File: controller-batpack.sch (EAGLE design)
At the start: 7 parts

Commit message: updated board with display and battery
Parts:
- removed 4D_LLC, RF_LLC: (no value), con-lstb:MA06-2
- removed BAT: SL-160AA/PR, battery:SL-160AA/PR
- removed RF_IC: MRF24J40, microchip:MRF24J40
- removed VD_R1: 1k, resistor:R-EU_0204/5
- removed VD_R2: 2k, resistor:R-EU_0204/5
- added G1: 5V, battery:SL-160AA/PR
- added JP1: (no value), pinhead:PINHD-1X8
- added R1: 2k, rcl:R-EU_0204/5
- added R2: 1k, rcl:R-EU_0204/5
- added U$1: LEVEL-SHIFTER-4CH, diy-modules:LEVEL-SHIFTER-4CH
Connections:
- removed net N$1: BAT.-, VD_R2.1
- removed net N$2: BAT.+, VD_R1.1
- removed net N$3: 4D_IC.1, RF_IC.VDD, VD_R1.2, VD_R2.2
- new net 3.3V: 4D_IC.1, R1.1, R2.2
- new net 4D_CS: JP1.4, U$1.HV2
- new net 4D_CS_L: 4D_IC.5, U$1.LV2
- new net 4D_INT: 4D_IC.6, JP1.5
- new net 4D_PD: JP1.3, U$1.HV1
- new net 4D_PD_L: 4D_IC.7, U$1.LV1
- new net 5V: G1.+, JP1.1, R2.1, U$1.HV
- new net GND: 4D_IC.10, G1.-, JP1.2, R1.2
- new net MISO: 4D_IC.3, JP1.6
- new net MOSI: JP1.7, U$1.HV3
- new net MOSI_L: 4D_IC.4, U$1.LV3
- new net N$10: U$1.LV
- new net SCK: JP1.8, U$1.HV4
- new net SCK_L: 4D_IC.2, U$1.LV4
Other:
- moved on the sheet: 4D_IC

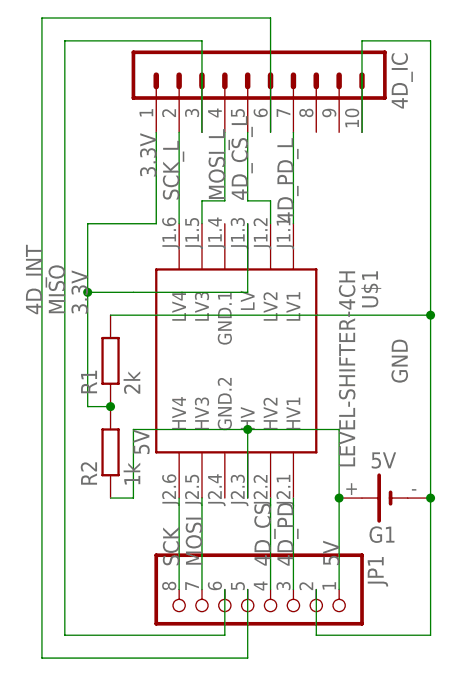
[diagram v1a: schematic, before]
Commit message: added pcb design and got rid of llc in battery pack
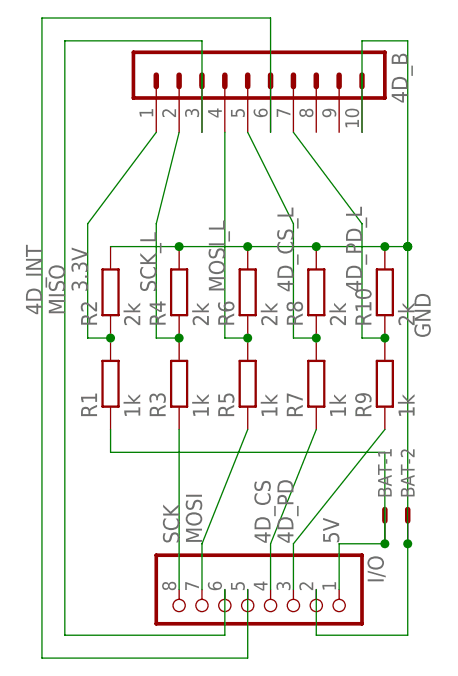
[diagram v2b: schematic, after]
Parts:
- removed G1: 5V, battery:SL-160AA/PR
- removed U$1: LEVEL-SHIFTER-4CH, diy-modules:LEVEL-SHIFTER-4CH
- added BAT: 22-23-2021, con-molex:22-23-2021
- added R10, R4, R6, R8: 2k, rcl:R-EU_M1206
- added R3, R5, R7, R9: 1k, rcl:R-EU_M1206
- R1: value 2k -> 1k; device rcl:R-EU_0204/5 -> rcl:R-EU_M1206
- R2: value 1k -> 2k; device rcl:R-EU_0204/5 -> rcl:R-EU_M1206
- renumbered 4D_IC to 4D_B, JP1 to I/O
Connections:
- removed net N$10: U$1.LV
- net 3.3V: now also R1.2, R2.1; no longer R1.1, R2.2
- net 4D_CS: now also R7.1; no longer U$1.HV2
- net 4D_CS_L: now also R7.2, R8.1; no longer U$1.LV2
- net 4D_PD: now also R9.1; no longer U$1.HV1
- net 4D_PD_L: now also R10.1, R9.2; no longer U$1.LV1
- net 5V: now also BAT-1.S, R1.1; no longer G1.+, R2.1, U$1.HV
- net GND: now also BAT-2.S, R10.2, R2.2, R4.2, R6.2, R8.2; no longer G1.-, R1.2
- net MOSI: now also R5.1; no longer U$1.HV3
- net MOSI_L: now also R5.2, R6.1; no longer U$1.LV3
- net SCK: now also R3.1; no longer U$1.HV4
- net SCK_L: now also R3.2, R4.1; no longer U$1.LV4
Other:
- moved on the sheet: R1, R2

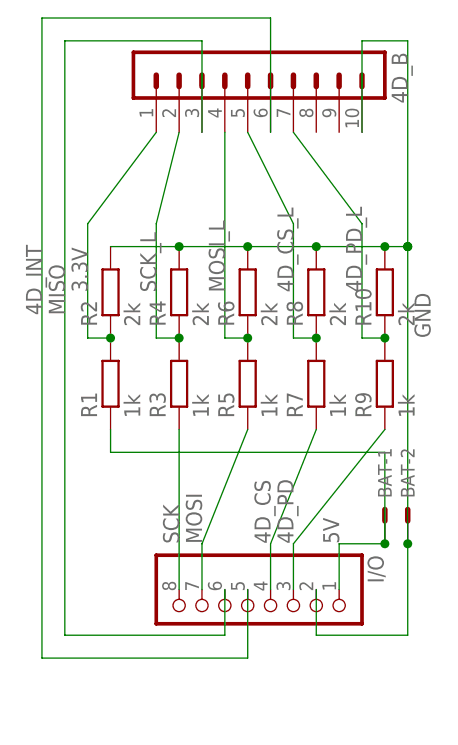
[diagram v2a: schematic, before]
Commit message: updated battery pack board
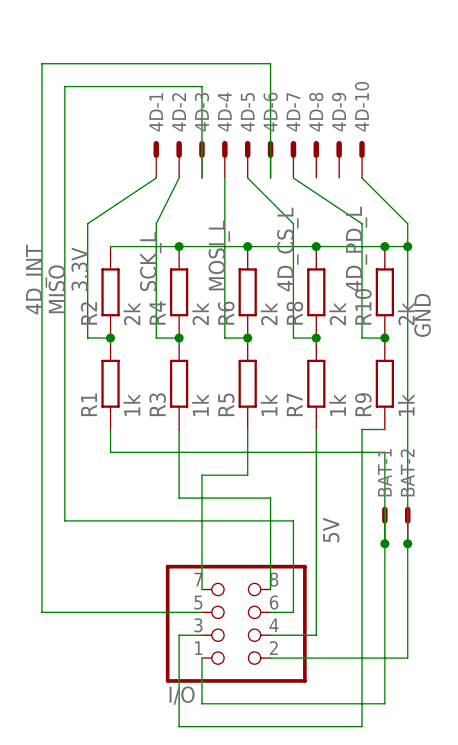
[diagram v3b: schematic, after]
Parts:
- removed 4D_B: (no value), con-lstb:MA10-1
- added 4D: 52745-1090, con-molex:52745-1090
- I/O: device pinhead:PINHD-1X8 -> pinhead:PINHD-2X4/90
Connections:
- net 3.3V: now also 4D-1.S; no longer 4D_B.1
- net 4D_CS_L: now also 4D-5.S; no longer 4D_B.5
- net 4D_INT: now also 4D-6.S; no longer 4D_B.6
- net 4D_PD_L: now also 4D-7.S; no longer 4D_B.7
- net GND: now also 4D-10.S; no longer 4D_B.10
- net MISO: now also 4D-3.S; no longer 4D_B.3
- net MOSI_L: now also 4D-4.S; no longer 4D_B.4
- net SCK_L: now also 4D-2.S; no longer 4D_B.2
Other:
- moved on the sheet: I/O

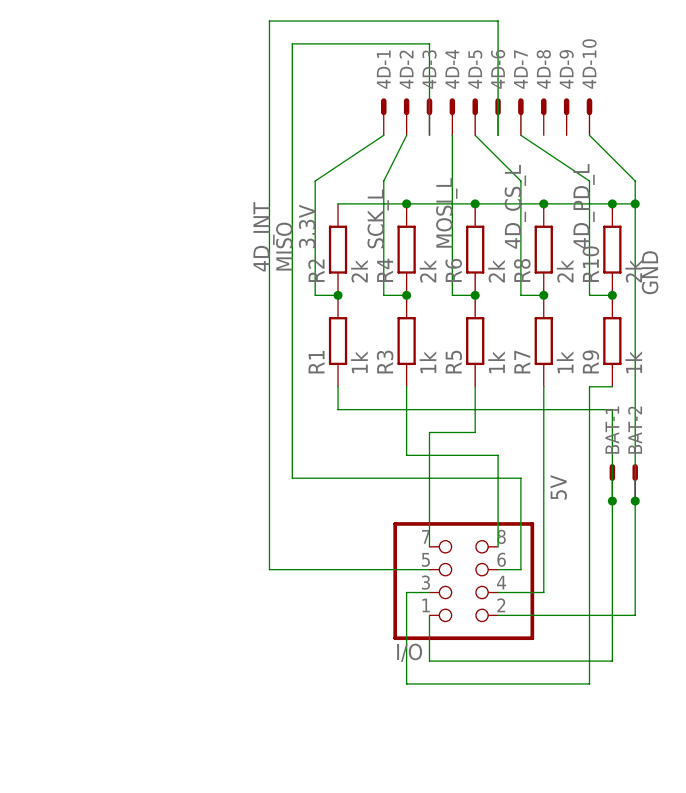
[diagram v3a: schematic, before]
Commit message: Created V2 main board, updated second board
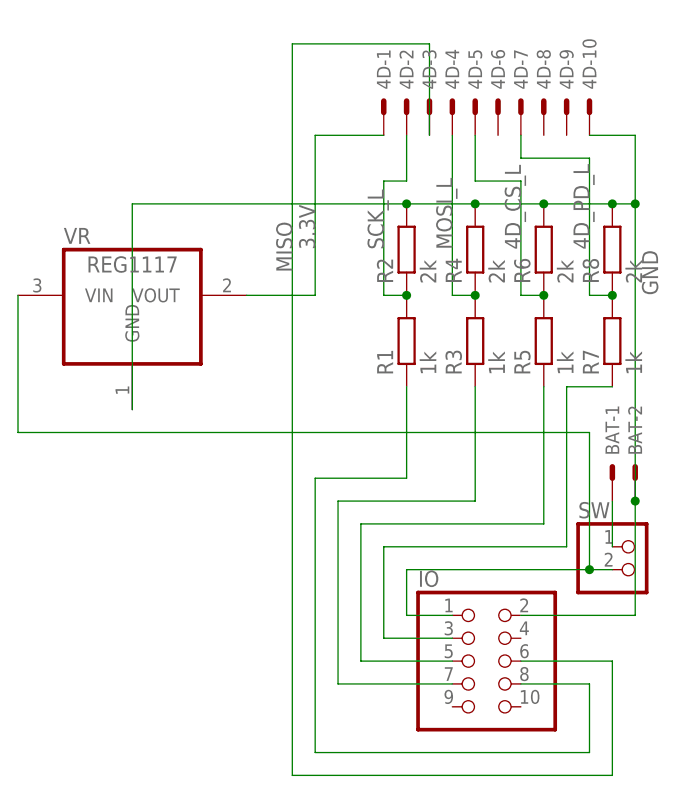
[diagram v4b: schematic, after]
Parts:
- removed I/O: (no value), pinhead:PINHD-2X4/90
- removed R10: 2k, rcl:R-EU_M1206
- removed R9: 1k, rcl:R-EU_M1206
- added IO: (no value), pinhead:PINHD-2X5/90
- added SW: (no value), pinhead:PINHD-1X2/90
- added VR: REG1117, burr-brown:REG1117
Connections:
- removed net 4D_INT: 4D-6.S, I/O.5
- new net 5V2: BAT-1.S, SW.1
- net 3.3V: now also VR.VOUT; no longer R1.2, R2.1
- net 4D_CS: now also IO.5, R5.1; no longer I/O.4, R7.1
- net 4D_CS_L: now also R5.2, R6.1; no longer R7.2, R8.1
- net 4D_PD: now also IO.3, R7.1; no longer I/O.3, R9.1
- net 4D_PD_L: now also R7.2, R8.1; no longer R10.1, R9.2
- net 5V: now also IO.1, SW.2, VR.VIN; no longer BAT-1.S, I/O.1, R1.1
- net GND: now also IO.2, VR.GND; no longer I/O.2, R10.2
- net MISO: now also IO.6; no longer I/O.6
- net MOSI: now also IO.7, R3.1; no longer I/O.7, R5.1
- net MOSI_L: now also R3.2, R4.1; no longer R5.2, R6.1
- net SCK: now also IO.8, R1.1; no longer I/O.8, R3.1
- net SCK_L: now also R1.2, R2.1; no longer R3.2, R4.1
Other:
- moved on the sheet: R1, R2, R3, R4, R5, R6, R7, R8
